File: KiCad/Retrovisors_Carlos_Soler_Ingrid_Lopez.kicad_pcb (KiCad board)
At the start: 2 copper layers, 125.5 x 100.5 mm, 121 parts, among them IC1 PIC24H, J1 Conn_01x02, J11 Conn_01x02, J12 Conn_01x02, J14 Conn_01x02_Pin, J2 DE9_Plug_MountingHoles, J3 DE9_Plug_MountingHoles, J3-4 Conn_01x02, J4 Conn_01x03, J5 Conn_01x02, J7 Conn_01x05, J7-8 Conn_01x02, J9 Conn_01x02, K1 G6E, K10 G6E, K2 G6E, K3 G6E, K4 G6E, K5 G6E, K6 G6E, K7 G6E, K8 G6E, K9 G6E, Q1 NMOS, Q10 NMOS, Q11 IRLZ44N, Q12 IRLZ44N, Q2 NMOS, Q3 NMOS, Q4 NMOS, Q5 NMOS, Q6 NMOS, Q7 NMOS, Q8 NMOS, Q9 NMOS, SW1 SW_DP3T, SW2 SW_DP3T, SW3 SW_DP3T, SW4 OP/CL, SW7 OP/CL, U1 TSR0.5-2450, U2 MCP2551-I-SN, U4 type="X" model="OPAMP" lib="", U5 type="X" model="OPAMP" lib="", U6 LM1117DT-3.3, Y1 Crystal

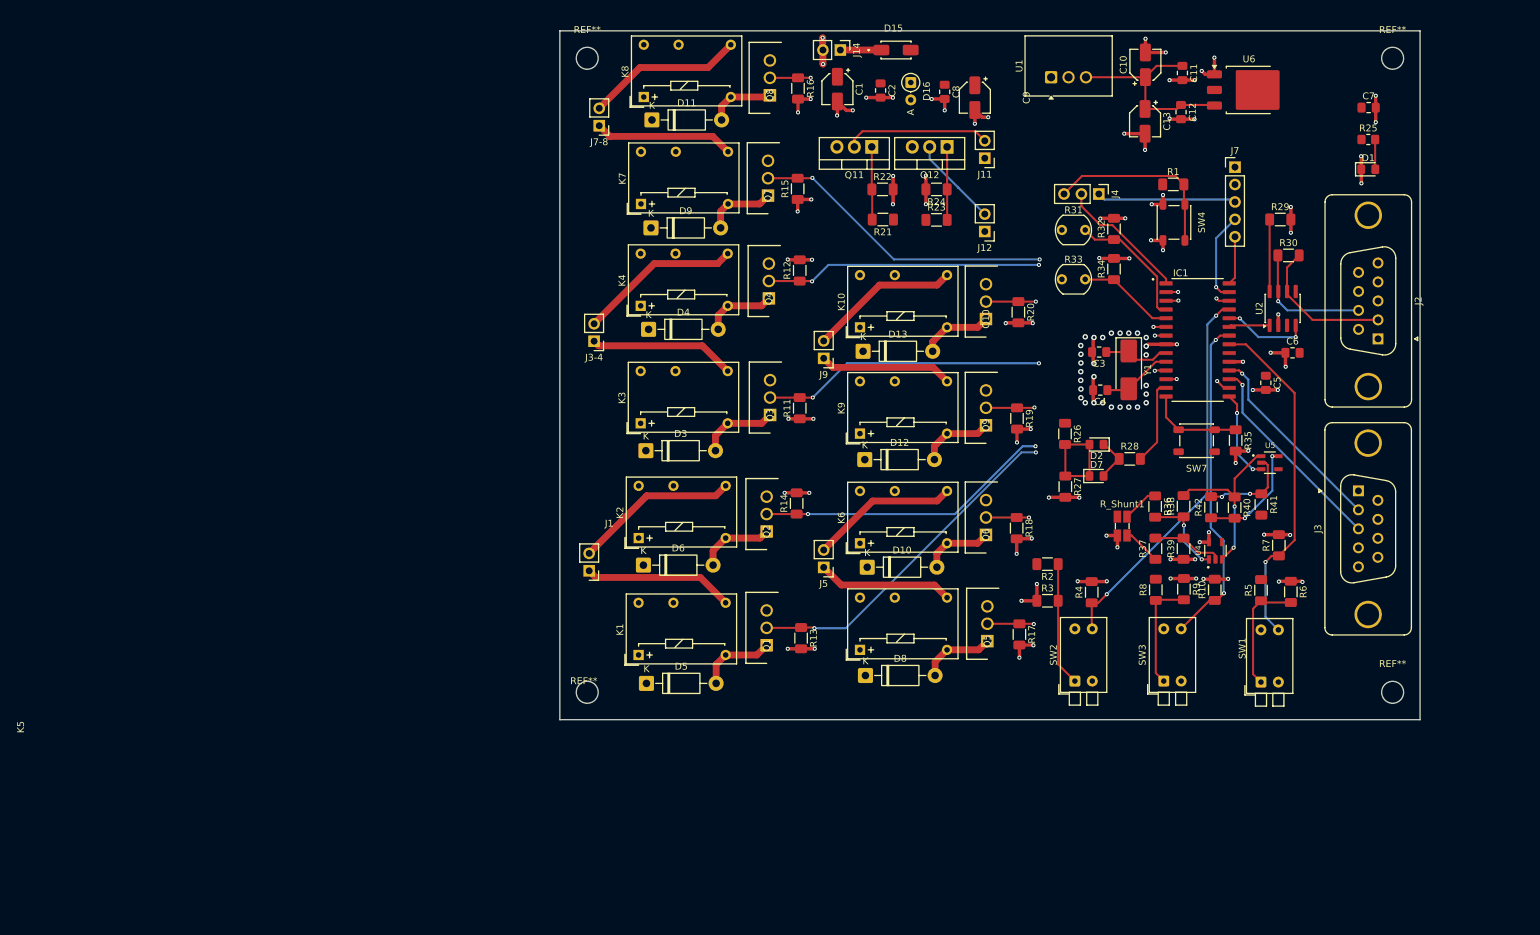
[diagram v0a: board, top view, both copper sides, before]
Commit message: canvis placement, afegir els r4emplazos que hi han a la pcb
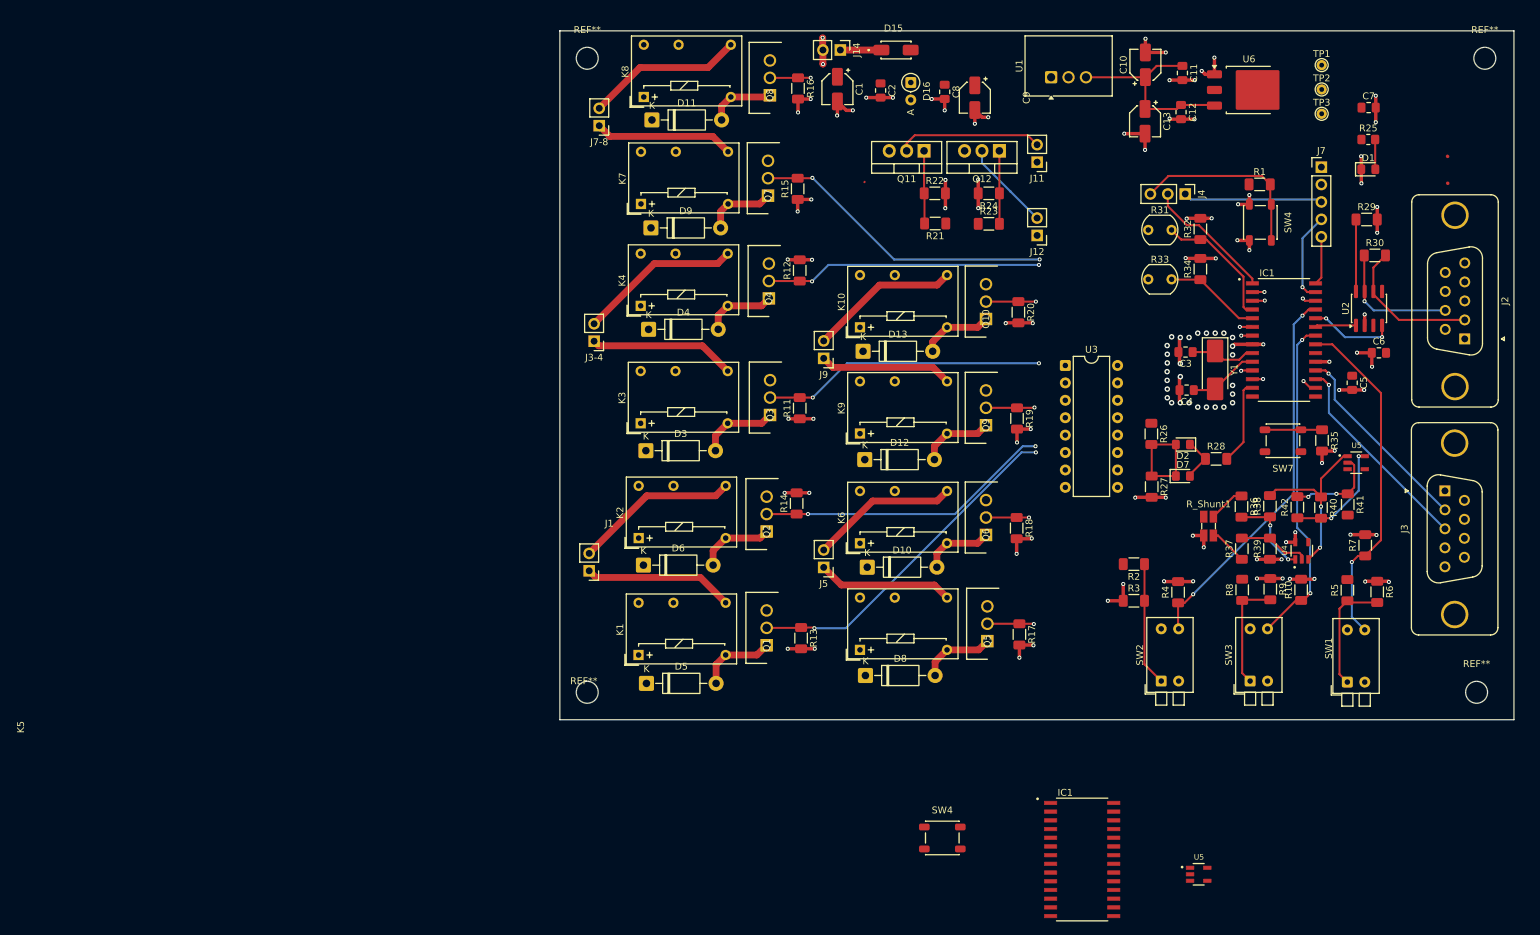
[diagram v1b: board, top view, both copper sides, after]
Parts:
- added IC1: PIC24H, AA_footprints:SOIC127P1030X265-28N, F.Cu at (127.2, 170.4)
- added SW4: OP/CL, Button_Switch_SMD:SW_SPST_PTS647_Sx38, F.Cu at (106.8, 167.2)
- added TP1: TestPoint, TestPoint:TestPoint_THTPad_D1.5mm_Drill0.7mm, F.Cu at (162.2, 54.5)
- added TP2: TestPoint, TestPoint:TestPoint_THTPad_D1.5mm_Drill0.7mm, F.Cu at (162.2, 58.0)
- added TP3: TestPoint-GND, TestPoint:TestPoint_THTPad_D1.5mm_Drill0.7mm, F.Cu at (162.2, 61.6)
- added U3: PCF8574P, Package_DIP:DIP-16_W7.62mm, F.Cu at (124.8, 98.3)
- added U5: type="X" model="OPAMP" lib="", AA_footprints:SOT95P280X145-5N, F.Cu at (144.2, 172.6)
- moved REF** 13.4 mm to (185.9, 53.5)
- moved J2 12.7 mm to (183.0, 94.4)
- moved J3 12.6 mm to (180.1, 116.6)
- moved J4 12.6 mm to (142.2, 73.3)
- moved R29 12.6 mm to (168.7, 77.0)
- moved R40 12.6 mm to (162.1, 119.0)
- moved R8 12.6 mm to (150.6, 131.1)
- moved SW1 12.6 mm to (165.9, 144.5)
- moved R26 12.6 mm to (137.3, 108.3)
- moved SW2 12.6 mm to (138.7, 144.4)
- moved C3 12.6 mm to (142.3, 96.4)
- moved C4 12.6 mm to (142.4, 101.9)
- moved C5 12.6 mm to (166.6, 100.8)
- moved C6 12.6 mm to (170.5, 96.5)
- moved D2 12.6 mm to (141.9, 109.8)
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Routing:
- net SC_IN: track 13.3 -> 0.00 mm, vias 2 -> 0
- net Net-(IC1-RC3/SCK/SCL): track 13.9 -> 8.32 mm
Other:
- board size 125.5 x 100.5 mm -> 139.2 x 100.5 mm

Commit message: correcions de pcb
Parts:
- removed the IC1 at (127.2, 170.4)
- removed the SW4 at (106.8, 167.2)
- removed the U5 at (144.2, 172.6)
- added R43: 4.7k, Resistor_SMD:R_1206_3216Metric_Pad1.30x1.75mm_HandSolder, F.Cu at (126.5, 92.0)
- added R44: 4.7k, Resistor_SMD:R_1206_3216Metric_Pad1.30x1.75mm_HandSolder, F.Cu at (132.0, 92.0)
- moved TP3 44.8 mm to (156.5, 106.0)
- moved D15 8.11 mm to (108.1, 53.0)
- moved J14 8.11 mm to (100.0, 53.0)
- moved TP1 6.87 mm to (169.0, 54.0)
- moved TP2 4.05 mm to (162.2, 54.0)
- moved J12 2.31 mm to (120.6, 77.0)
- moved C11 2.23 mm to (141.7, 57.9)
- moved C13 2.23 mm to (136.3, 64.9)
- moved C10 2.23 mm to (136.3, 56.7)
- moved C12 2.23 mm to (141.5, 63.6)
- moved U1 2.23 mm to (122.6, 58.5)
- moved U6 2.23 mm to (151.5, 60.4)
- moved C9 1.31 mm to (112.8, 59.5)
- moved C2 1.31 mm to (99.1, 58.5)
- moved C1 1.31 mm to (92.8, 58.3)
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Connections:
- net /CAN+ renamed /Digital/CAN+
- net /CAN- renamed /Digital/CAN-
- net /Vdrain1 renamed /Potencia/Vdrain1
- net /Vdrain3 renamed /Potencia/Vdrain3
- net /Vdrain4 renamed /Potencia/Vdrain4
- C8 pad 2: GNDPWR -> GND
- C9 pad 2: GNDPWR -> GND
- D10 pad 2: /Vdrain2 -> Net-(D10-A)
- D13 pad 2: /Vdrain2 -> /Potencia/Vdrain2
- D16 pad 2: GNDPWR -> GND
- D6 pad 2: /Vdrain2 -> /Potencia/Vdrain2
- IC1 pad 11: DM_O -> Net-(IC1-RC0/T1OSO/T13CKI)
- IC1 pad 12: DM_C -> SC_IN
- IC1 pad 15: SC_IN -> Net-(IC1-RC4/SDI/SDA)
- IC1 pad 16: CAL_R -> unconnected-(IC1-RC5/SDO-Pad16)
- IC1 pad 17: /TX -> /Digital/TX
- IC1 pad 18: /RX -> /Digital/RX
- IC1 pad 2: DLY_U -> CAL_L
- IC1 pad 26: CAL_L -> unconnected-(IC1-RB5/KBI1/PGM-Pad26)
- IC1 pad 3: DLY_D -> CAL_R
- IC1 pad 6: DLX_U -> DRY_D
- IC1 pad 7: DLX_D -> DRY_U
- J14 pad 2: GNDPWR -> GND
- J3 pad 2: /RX -> /Digital/RX
- J3 pad 3: /TX -> /Digital/TX
- K1 pad 10: GNDPWR -> GND
- K10 pad 6: /Vdrain2 -> /Potencia/Vdrain2
- K2 pad 10: GNDPWR -> GND
- K2 pad 6: /Vdrain2 -> /Potencia/Vdrain2
- K3 pad 10: GNDPWR -> GND
- K4 pad 10: GNDPWR -> GND
- K5 pad 10: GNDPWR -> GND
- K6 pad 10: GNDPWR -> GND
- K6 pad 6: /Vdrain2 -> Net-(D10-A)
- K7 pad 10: GNDPWR -> GND
- K8 pad 10: GNDPWR -> GND
- Q1 pad 3: GNDPWR -> GND
- Q10 pad 1: /Vdrain2 -> /Potencia/Vdrain2
- Q10 pad 3: GNDPWR -> GND
- Q2 pad 1: /Vdrain2 -> /Potencia/Vdrain2
- Q2 pad 3: GNDPWR -> GND
- Q3 pad 3: GNDPWR -> GND
- Q4 pad 3: GNDPWR -> GND
- Q5 pad 3: GNDPWR -> GND
- Q6 pad 1: /Vdrain2 -> Net-(D10-A)
- Q6 pad 3: GNDPWR -> GND
- Q7 pad 3: GNDPWR -> GND
- Q8 pad 3: GNDPWR -> GND
- Q9 pad 3: GNDPWR -> GND
- R35 pad 1: Net-(IC1-RC3/SCK/SCL) -> Net-(IC1-RC0/T1OSO/T13CKI)
- SW7 pad 2: Net-(IC1-RC3/SCK/SCL) -> Net-(IC1-RC0/T1OSO/T13CKI)
- U1 pad 2: GNDPWR -> GND
- U3 pad 10: DRX_U -> DLX_U
- U3 pad 11: DRY_D -> DRX_D
- U3 pad 12: DRY_U -> DRX_U
- U3 pad 4: DLX_D -> DLY_D
- U3 pad 5: DLX_U -> DLY_U
- U3 pad 6: DLY_D -> DM_O
- U3 pad 7: DLY_U -> DM_C
- U3 pad 9: DRX_D -> DLX_D
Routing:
- net DRY_D: track 6.05 -> 93.2 mm, vias 1 -> 3
- net CAL_L: track 1.99 -> 49.0 mm, vias 1 -> 2
- net DLX_U: track 52.0 -> 7.18 mm, vias 3 -> 1
- net CAL_R: track 2.16 -> 45.9 mm, vias 1 -> 2
- net DLX_D: track 45.0 -> 6.03 mm, vias 3 -> 1
- net DRY_U: track 44.6 -> 80.2 mm, vias 2 -> 3
- net Net-(IC1-RC4/SDI/SDA): track 0.00 -> 32.7 mm, vias 0 -> 1
- net /Vdrain2: track 32.1 -> 0.00 mm
- net /TX: track 30.3 -> 0.00 mm, vias 1 -> 0
- net /Digital/TX: track 0.00 -> 30.3 mm, vias 0 -> 1
- net /RX: track 29.0 -> 0.00 mm, vias 1 -> 0
- net /Digital/RX: track 0.00 -> 29.0 mm, vias 0 -> 1
- net DM_C: track 8.84 -> 33.6 mm
- net DLY_D: track 42.2 -> 64.8 mm, vias 3 -> 2
- net SC_IN: track 0.00 -> 22.2 mm, vias 0 -> 2
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- added copper zone on B.Cu, net GND
- added copper zone on F.Cu, net GND
- added copper zone on F.Cu, net VBAT_PROT
- added copper zone on F.Cu, net VCC

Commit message: placa abans de canvi placement 1
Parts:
- moved C1 69.8 mm to (162.6, 61.0)
- moved C2 58.4 mm to (157.5, 61.0)
- moved J2 10.9 mm to (180.0, 83.9), turned to 90 degrees
- moved D15 10.4 mm to (98.6, 57.1)
- moved J14 3.50 mm to (96.5, 53.3), turned to 90 degrees
- moved D16 0.65 mm to (104.1, 57.3)
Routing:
- net GND: track 170.6 -> 161.6 mm, vias 117 -> 113
- net /Digital/CAN-: track 21.2 -> 16.8 mm
- net /Digital/CAN+: track 19.3 -> 23.0 mm, vias 1 -> 2
- net +12V: track 5.99 -> 3.78 mm
- removed copper zone on F.Cu, net VBAT_PROT
